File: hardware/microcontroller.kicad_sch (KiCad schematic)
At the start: 1 part, among them U1 STM32G474QBTx

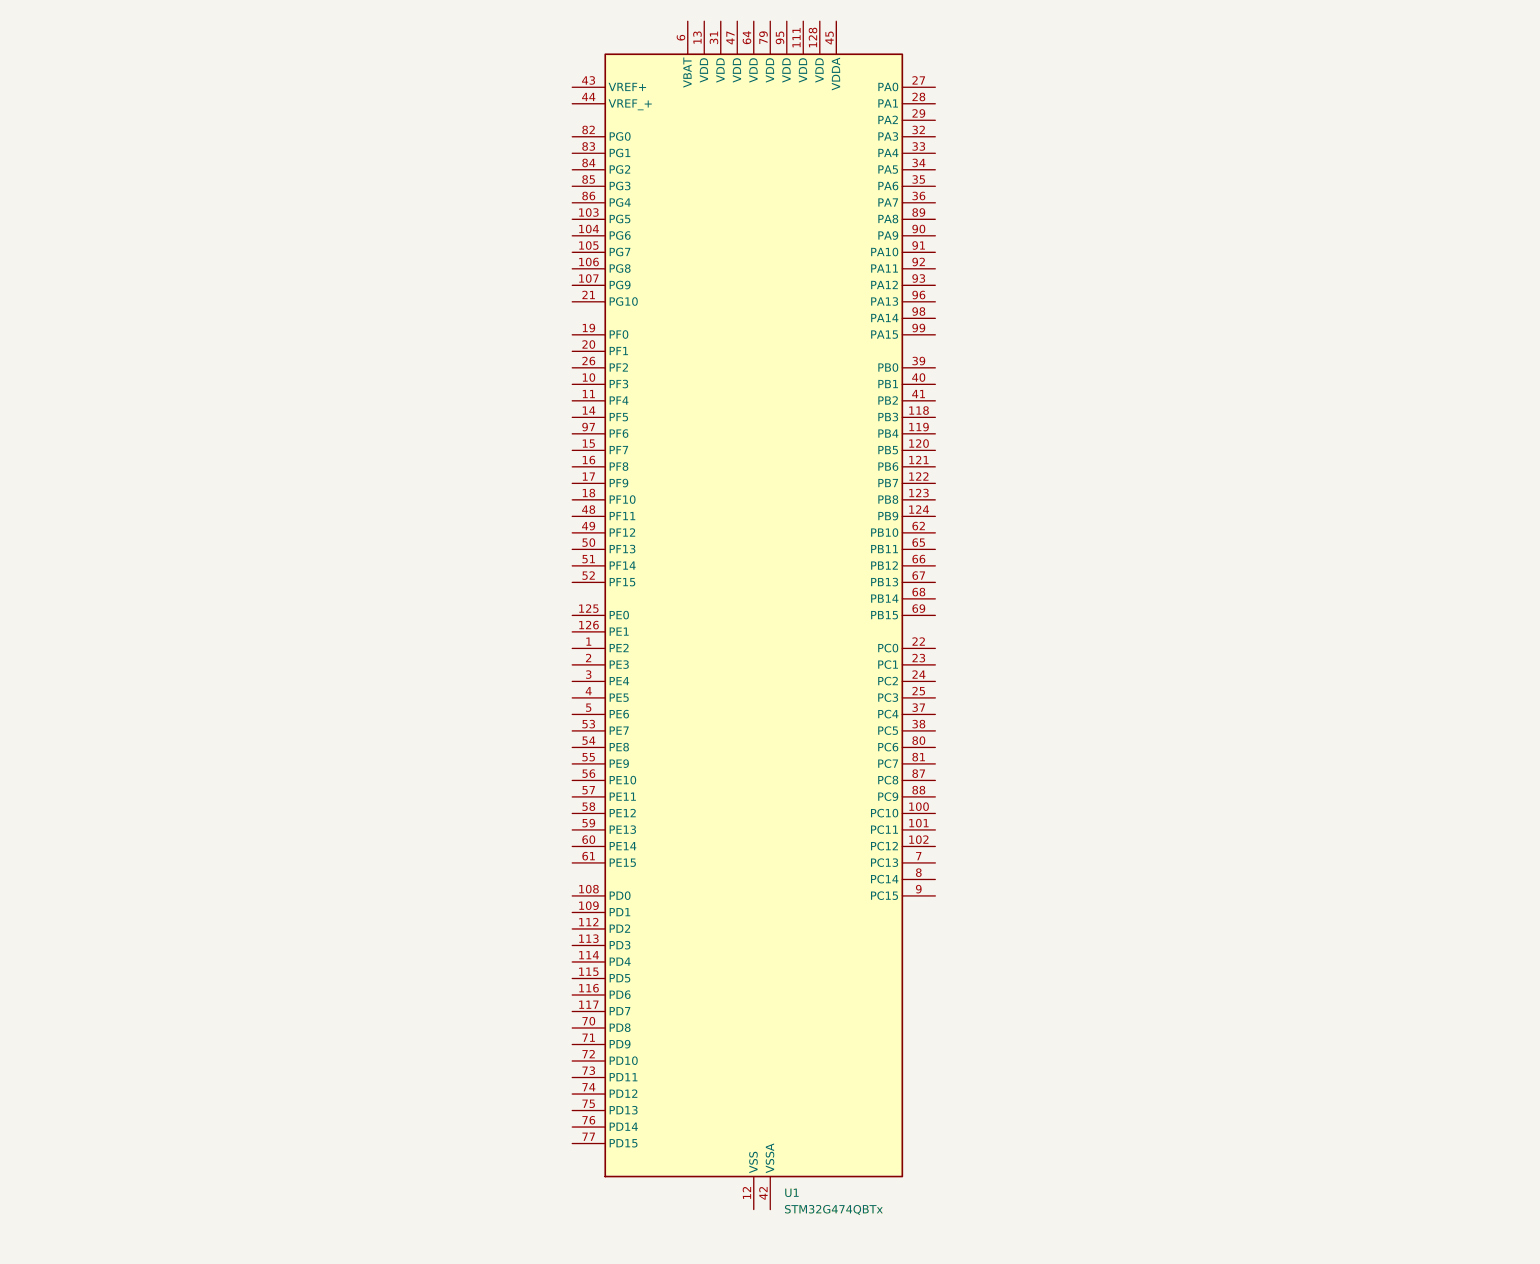
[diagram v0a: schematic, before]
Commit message: Add 3.3V buck converter
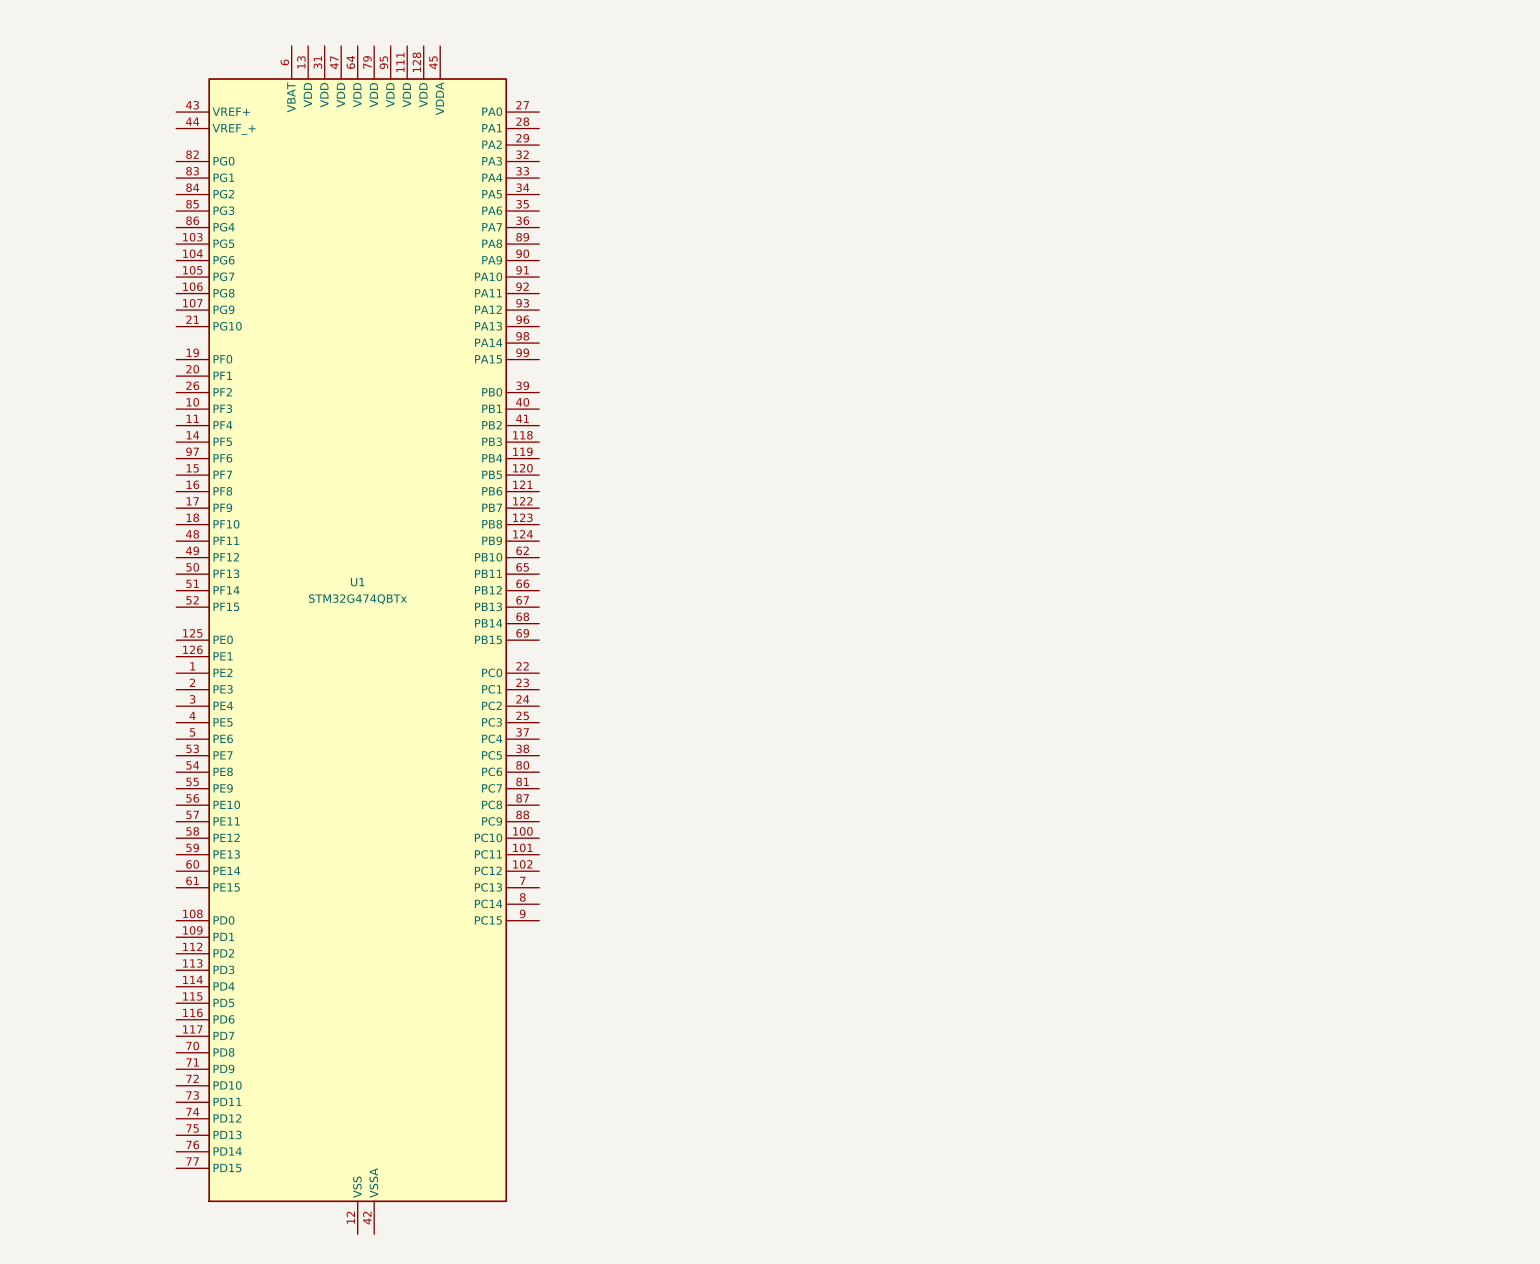
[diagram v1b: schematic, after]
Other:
- moved on the sheet: U1
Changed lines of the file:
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@@
 	(generator "eeschema")
 	(generator_version "10.0")
-	(paper "A4")
+	(paper "A")
 	(symbol
 		(lib_id "MCU_ST_STM32G4:STM32G474QBTx")
-		(at 144.78 105.41 0)
+		(at 83.82 109.22 0)
 		(unit 1)
 		(body_style 1)
@@
 		(in_pos_files yes)
 		(dnp no)
-		(fields_autoplaced yes)
 		(property "Reference" "U1"
-			(at 149.4633 194.31 0)
+			(at 83.82 100.33 0)
 			(show_name no)
 			(do_not_autoplace no)
@@
 					(size 1.27 1.27)
 				)
-				(justify left)
 			)
 		)
 		(property "Value" "STM32G474QBTx"
-			(at 149.4633 196.85 0)
+			(at 83.82 102.87 0)
 			(show_name no)
 			(do_not_autoplace no)
@@
 					(size 1.27 1.27)
 				)
-				(justify left)
 			)
 		)
 		(property "Footprint" "Package_QFP:LQFP-128_14x14mm_P0.4mm"
-			(at 121.92 191.77 0)
+			(at 60.96 195.58 0)
 			(hide yes)
 			(show_name no)
@@
 		)
 		(property "Datasheet" "https://www.st.com/resource/en/datasheet/stm32g474qb.pdf"
-			(at 144.78 105.41 0)
+			(at 83.82 109.22 0)
 			(hide yes)
 			(show_name no)
@@
 		)
 		(property "Description" "STMicroelectronics Arm Cortex-M4 MCU, 128KB flash, 128KB RAM, 170 MHz, 1.71-3.6V, 107 GPIO, LQFP128"
-			(at 144.78 105.41 0)
+			(at 83.82 109.22 0)
 			(hide yes)
 			(show_name no)

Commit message: Create MCU schematic
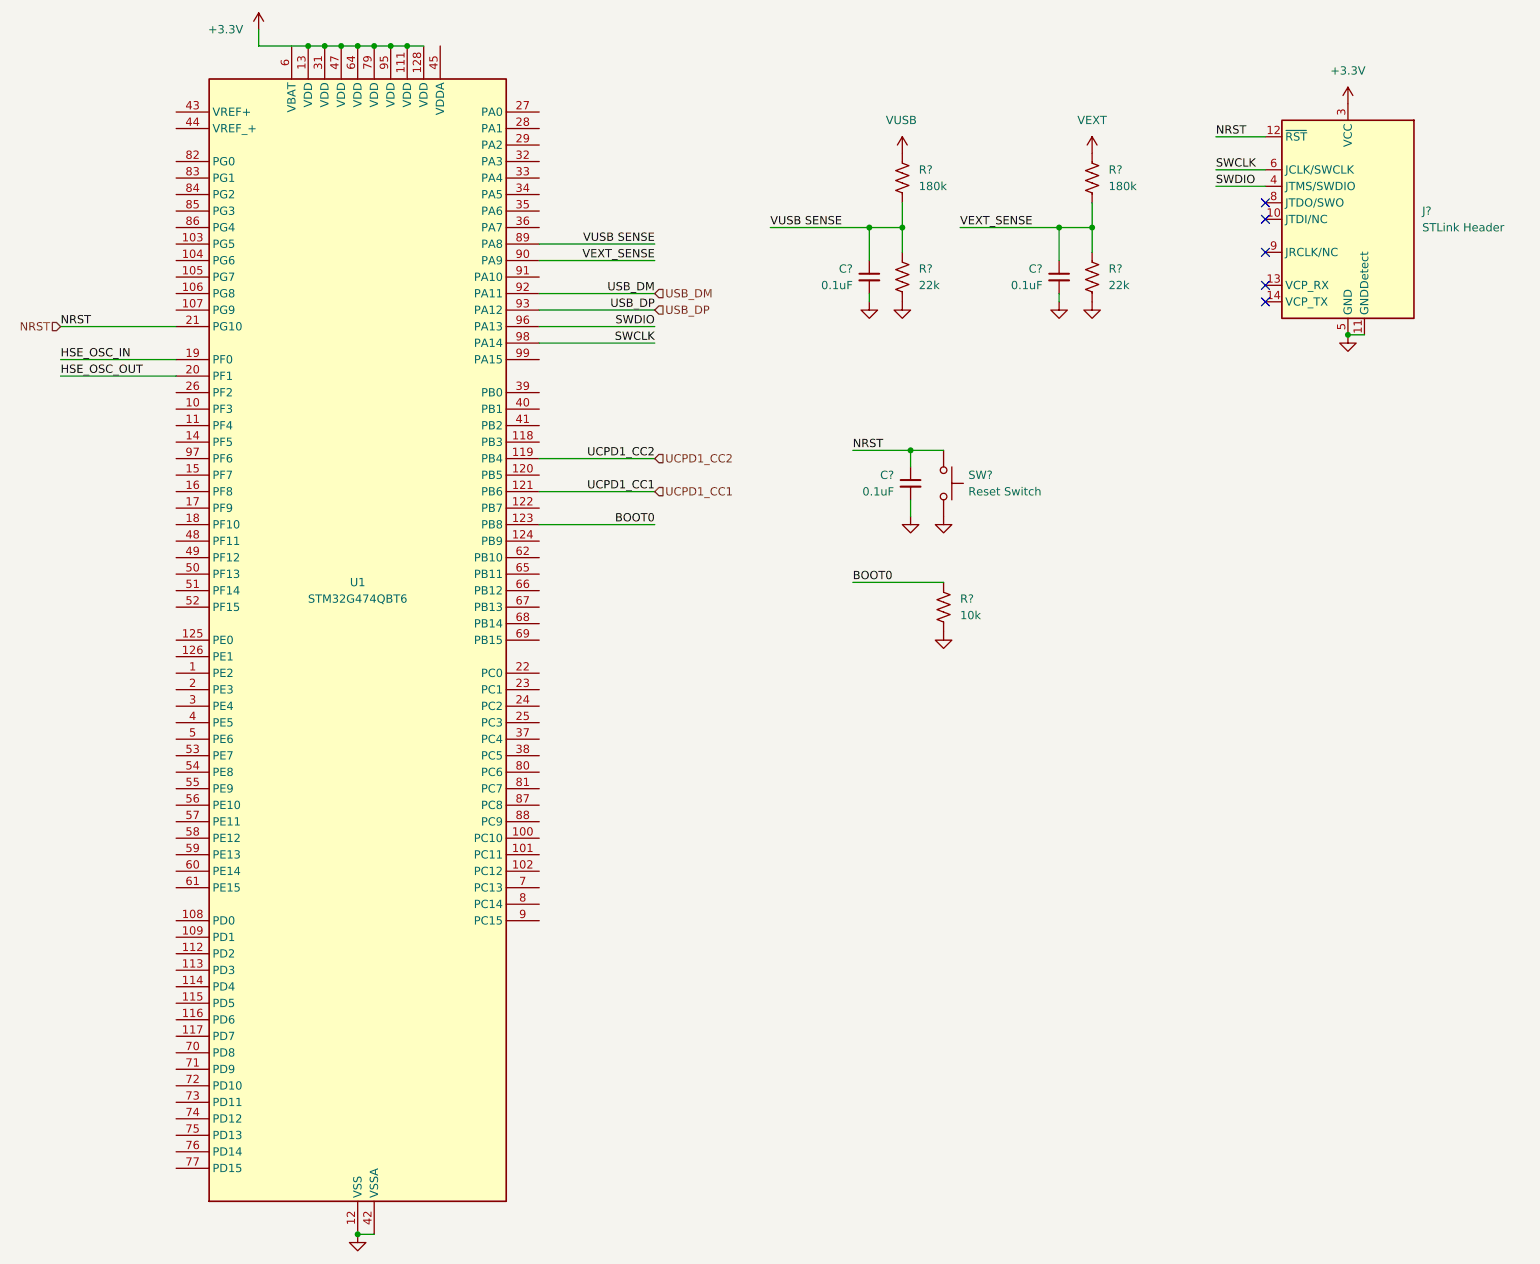
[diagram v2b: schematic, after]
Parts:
- added C? (x3): 0.1uF, Capacitor_SMD:C_0603_1608Metric_Pad1.08x0.95mm_HandSolder, symbol Device:C_Small
- added J?: STLink Header, Connector_PinHeader_1.27mm:PinHeader_2x07_P1.27mm_Vertical_SMD, symbol Connector:Conn_ST_STDC14
- added R? (x2): 180k, symbol Device:R_US
- added R? (x2): 22k, symbol Device:R_US
- added R?: 10k, symbol Device:R_US
- added SW?: Reset Switch, Button_Switch_SMD:SW_SPST_PTS647_Sx38, symbol Switch:SW_Push
- U1: value STM32G474QBTx -> STM32G474QBT6; Part Number (none) -> STM32G474QBT6; Vendor URL (none) -> https://www.digikey.com/en/products/detail/stmicroelectroni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
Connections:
- net GND: now reaches U1.110 (VSS), U1.12 (VSS), U1.127 (VSS), U1.30 (VSS), U1.46 (VSS), U1.63 (VSS), U1.78 (VSS), U1.94 (VSS)
- net GND: now also U1.42 (VSSA), C?.2, C?.2, C?.2, J?.11 (GNDDetect), J?.5 (GND), J?.7 (GND), R?.2, R?.2, R?.2, SW?.2
- net +3.3V: now reaches U1.111 (VDD)
- net +3.3V: now also U1.128 (VDD), U1.13 (VDD), U1.31 (VDD), U1.47 (VDD), U1.64 (VDD), U1.79 (VDD), U1.95 (VDD), J?.3 (VCC)
- net UCPD1_CC2: now reaches U1.119 (PB4)
- net UCPD1_CC1: now reaches U1.121 (PB6)
- net BOOT0: now reaches U1.123 (PB8)
- net BOOT0: now also R?.1
- net HSE_OSC_IN: now reaches U1.19 (PF0)
- net HSE_OSC_OUT: now reaches U1.20 (PF1)
- net NRST: now reaches U1.21 (PG10)
- net NRST: now also C?.1, J?.12 (~{RST}), SW?.1
- net VUSB SENSE: now reaches U1.89 (PA8)
- net VUSB SENSE: now also C?.1, R?.1, R?.2
- net VEXT_SENSE: now reaches U1.90 (PA9)
- net VEXT_SENSE: now also C?.1, R?.1, R?.2
- net USB_DM: now reaches U1.92 (PA11)
- net USB_DP: now reaches U1.93 (PA12)
- net SWDIO: now reaches U1.96 (PA13)
- net SWDIO: now also J?.4 (JTMS/SWDIO)
- net SWCLK: now reaches U1.98 (PA14)
- net SWCLK: now also J?.6 (JCLK/SWCLK)
- new net VEXT: R?.1
- new net VUSB: R?.1
- no-connect marks 0 -> 5
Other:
- company: (none) -> Jacob Wigent
- title: (none) -> STM32G4 Microcontroller
